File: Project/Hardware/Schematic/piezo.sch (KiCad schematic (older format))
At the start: 5 parts

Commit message: Fixa bibliotek ref
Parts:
- U?: symbol lab-rescue:piezo-PASC -> PASC:piezo
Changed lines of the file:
@@
 $EndDescr
 $Comp
-L lab-rescue:piezo-PASC U?
+L PASC:piezo U?
 U 1 1 5C5E3EC0
 P 6600 3700

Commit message: La till pins till cubemx, bytte transistor till piezo och la till footprint för accelerometer
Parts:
- removed Q?: 2SC1815, Package_TO_SOT_THT:TO-92_Inline, symbol Transistor_BJT:2SC1815
- added Q?: 2N3906, Package_TO_SOT_THT:TO-92_Inline, symbol Transistor_BJT:2N3906
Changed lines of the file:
@@
 	0    1    1    0
-$EndComp
-$Comp
-L Transistor_BJT:2SC1815 Q?
-U 1 1 5C5EB691
-P 5600 4600
-F 0 "Q?" H 5791 4646 50  0000 L CNN
-F 1 "2SC1815" H 5791 4555 50  0000 L CNN
-F 2 "Package_TO_SOT_THT:TO-92_Inline" H 5800 4525 50  0001 L CIN
-F 3 "https://media.digikey.com/pdf/Data%20Sheets/Toshiba%20PDFs/2SC1815.pdf" H 5600 4600 50  0001 L CNN
-	1    5600 4600
-	1    0    0    -1
 $EndComp
 Wire Wire Line
@@
 Text HLabel 4300 4600 0    50   Input ~ 0
 PIEZOPWM
+$Comp
+L Transistor_BJT:2N3906 Q?
+U 1 1 5C68E108
+P 5600 4600
+F 0 "Q?" H 5791 4646 50  0000 L CNN
+F 1 "2N3906" H 5791 4555 50  0000 L CNN
+F 2 "Package_TO_SOT_THT:TO-92_Inline" H 5800 4525 50  0001 L CIN
+F 3 "https://www.fairchildsemi.com/datasheets/2N/2N3906.pdf" H 5600 4600 50  0001 L CNN
+	1    5600 4600
+	1    0    0    -1
+$EndComp
 $EndSCHEMATC

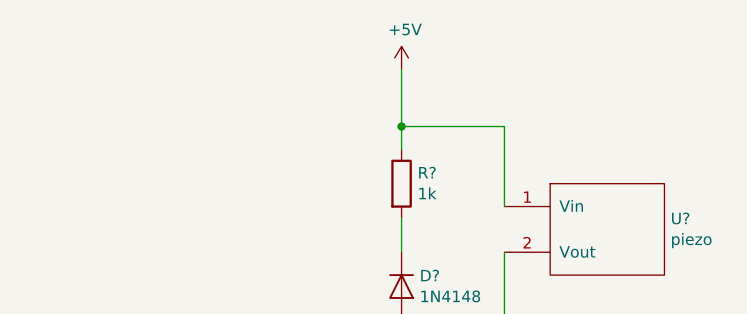
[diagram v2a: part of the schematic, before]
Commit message: Tagit bort knapp, ändrat power till piezo
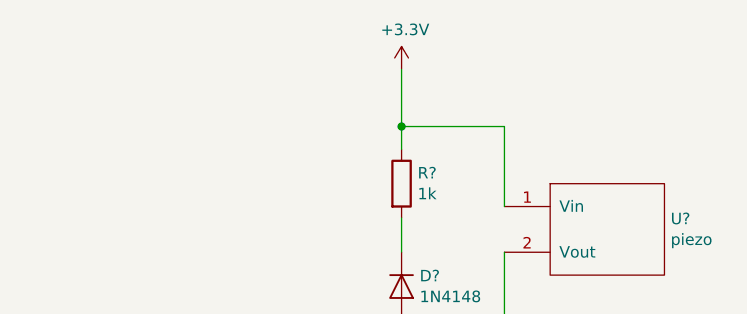
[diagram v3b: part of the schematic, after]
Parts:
- Q?: footprint Package_TO_SOT_THT:TO-92_Inline -> TO_SOT_Packages_THT:TO-92_Inline_Wide
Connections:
- net +5V renamed +3V3
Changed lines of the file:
@@
 Wire Wire Line
 	4750 4600 4300 4600
-$Comp
-L power:+5V #PWR?
-U 1 1 5C5E2E3F
-P 5700 3000
-F 0 "#PWR?" H 5700 2850 50  0001 C CNN
-F 1 "+5V" H 5715 3173 50  0000 C CNN
-F 2 "" H 5700 3000 50  0001 C CNN
-F 3 "" H 5700 3000 50  0001 C CNN
-	1    5700 3000
-	1    0    0    -1
-$EndComp
 Text HLabel 4300 4600 0    50   Input ~ 0
 PIEZOPWM
@@
 F 0 "Q?" H 5791 4646 50  0000 L CNN
 F 1 "2N3906" H 5791 4555 50  0000 L CNN
-F 2 "Package_TO_SOT_THT:TO-92_Inline" H 5800 4525 50  0001 L CIN
+F 2 "TO_SOT_Packages_THT:TO-92_Inline_Wide" H 5800 4525 50  0001 L CIN
 F 3 "https://www.fairchildsemi.com/datasheets/2N/2N3906.pdf" H 5600 4600 50  0001 L CNN
 	1    5600 4600
 	1    0    0    -1
 $EndComp
+$Comp
+L power:+3.3V #PWR?
+U 1 1 5C6DC10D
+P 5700 3000
+F 0 "#PWR?" H 5700 2850 50  0001 C CNN
+F 1 "+3.3V" H 5715 3173 50  0000 C CNN
+F 2 "" H 5700 3000 50  0001 C CNN
+F 3 "" H 5700 3000 50  0001 C CNN
+	1    5700 3000
+	1    0    0    -1
+$EndComp

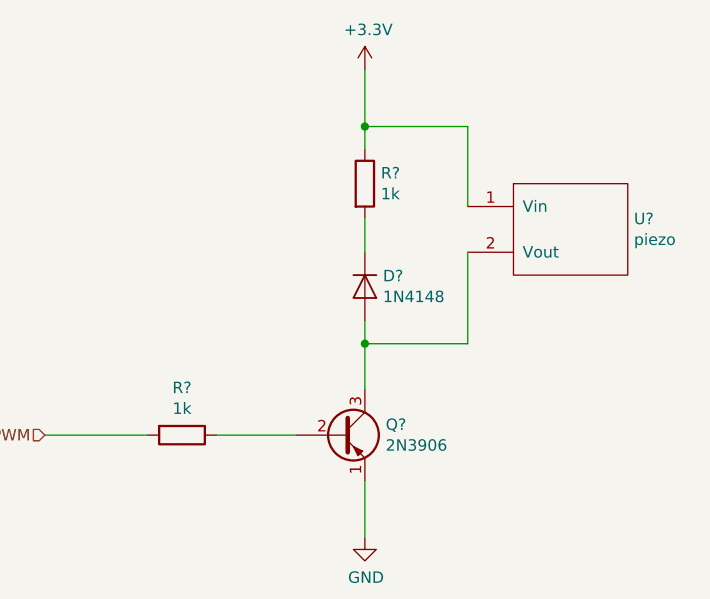
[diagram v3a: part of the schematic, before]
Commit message: Tog bort power supply +7, lade till switch för att switcha mellan batteri och USB power. Lade till power-net symbol för oregulerad supply voltage +VIN.
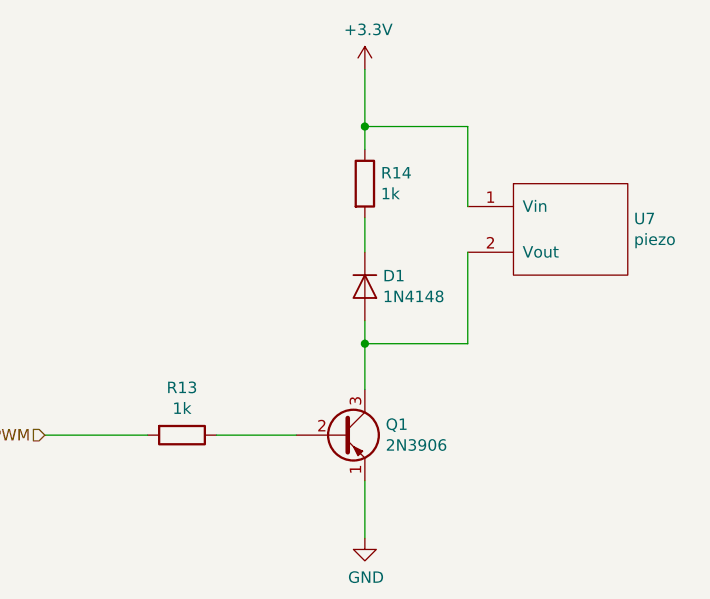
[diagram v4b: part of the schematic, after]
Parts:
- gave numbers to parts that had none: 5
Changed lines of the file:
@@
 $EndDescr
 $Comp
-L PASC:piezo U?
+L PASC:piezo U7
 U 1 1 5C5E3EC0
 P 6600 3700
-F 0 "U?" H 6877 3746 50  0000 L CNN
+F 0 "U7" H 6877 3746 50  0000 L CNN
 F 1 "piezo" H 6877 3655 50  0000 L CNN
 F 2 "PASC:Piezo" H 6600 3700 50  0001 C CNN
@@
 $EndComp
 $Comp
-L Device:R R?
+L Device:R R14
 U 1 1 5C5EB38A
 P 5700 3500
-F 0 "R?" H 5770 3546 50  0000 L CNN
+F 0 "R14" H 5770 3546 50  0000 L CNN
 F 1 "1k" H 5770 3455 50  0000 L CNN
 F 2 "" V 5630 3500 50  0001 C CNN
@@
 $EndComp
 $Comp
-L Diode:1N4148 D?
+L Diode:1N4148 D1
 U 1 1 5C5EB4E1
 P 5700 3950
-F 0 "D?" V 5654 4029 50  0000 L CNN
+F 0 "D1" V 5654 4029 50  0000 L CNN
 F 1 "1N4148" V 5745 4029 50  0000 L CNN
 F 2 "Diode_THT:D_DO-35_SOD27_P7.62mm_Horizontal" H 5700 3775 50  0001 C CNN
@@
 	5700 4200 5700 4400
 $Comp
-L Device:R R?
+L Device:R R13
 U 1 1 5C5EB823
 P 4900 4600
-F 0 "R?" V 4693 4600 50  0000 C CNN
+F 0 "R13" V 4693 4600 50  0000 C CNN
 F 1 "1k" V 4784 4600 50  0000 C CNN
 F 2 "" V 4830 4600 50  0001 C CNN
@@
 	5050 4600 5400 4600
 $Comp
-L power:GND #PWR?
+L power:GND #PWR0137
 U 1 1 5C5EB928
 P 5700 5050
-F 0 "#PWR?" H 5700 4800 50  0001 C CNN
+F 0 "#PWR0137" H 5700 4800 50  0001 C CNN
 F 1 "GND" H 5705 4877 50  0000 C CNN
 F 2 "" H 5700 5050 50  0001 C CNN
@@
 PIEZOPWM
 $Comp
-L Transistor_BJT:2N3906 Q?
+L Transistor_BJT:2N3906 Q1
 U 1 1 5C68E108
 P 5600 4600
-F 0 "Q?" H 5791 4646 50  0000 L CNN
+F 0 "Q1" H 5791 4646 50  0000 L CNN
 F 1 "2N3906" H 5791 4555 50  0000 L CNN
 F 2 "TO_SOT_Packages_THT:TO-92_Inline_Wide" H 5800 4525 50  0001 L CIN
@@
 $EndComp
 $Comp
-L power:+3.3V #PWR?
+L power:+3.3V #PWR0138
 U 1 1 5C6DC10D
 P 5700 3000
-F 0 "#PWR?" H 5700 2850 50  0001 C CNN
+F 0 "#PWR0138" H 5700 2850 50  0001 C CNN
 F 1 "+3.3V" H 5715 3173 50  0000 C CNN
 F 2 "" H 5700 3000 50  0001 C CNN

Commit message: Intermediate...
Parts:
- removed Q1: 2N3906, TO_SOT_Packages_THT:TO-92_Inline_Wide, symbol Transistor_BJT:2N3906
- added Q1: 2N3904, Package_TO_SOT_THT:TO-92_Inline_Wide, symbol Transistor_BJT:2N3904
- R13, R14: footprint (none) -> Resistor_SMD:R_0805_2012Metric_Pad1.15x1.40mm_HandSolder
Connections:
- net GND: now also Q1.1 (E)
- net at D1.2 (A), U7.2 (Vout): now also Q1.3 (C)
- net at R13.1: now also Q1.2 (B)
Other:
- moved on the sheet: D1, R13, R14, U7
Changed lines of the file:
@@
 EELAYER 26 0
 EELAYER END
-$Descr A4 11693 8268
+$Descr User 5512 5512
 encoding utf-8
 Sheet 6 7
 Title ""
-Date ""
-Rev ""
-Comp ""
+Date "2019-02-12"
+Rev "1"
+Comp "PASC"
 Comment1 ""
 Comment2 ""
@@
 L PASC:piezo U7
 U 1 1 5C5E3EC0
-P 6600 3700
-F 0 "U7" H 6877 3746 50  0000 L CNN
-F 1 "piezo" H 6877 3655 50  0000 L CNN
-F 2 "PASC:Piezo" H 6600 3700 50  0001 C CNN
-F 3 "" H 6600 3700 50  0001 C CNN
-	1    6600 3700
+P 3800 1800
+F 0 "U7" H 4077 1846 50  0000 L CNN
+F 1 "piezo" H 4077 1755 50  0000 L CNN
+F 2 "PASC:Piezo" H 3800 1800 50  0001 C CNN
+F 3 "" H 3800 1800 50  0001 C CNN
+	1    3800 1800
 	1    0    0    -1
 $EndComp
@@
 L Device:R R14
 U 1 1 5C5EB38A
-P 5700 3500
-F 0 "R14" H 5770 3546 50  0000 L CNN
-F 1 "1k" H 5770 3455 50  0000 L CNN
-F 2 "" V 5630 3500 50  0001 C CNN
-F 3 "~" H 5700 3500 50  0001 C CNN
-	1    5700 3500
+P 2900 1600
+F 0 "R14" H 2970 1646 50  0000 L CNN
+F 1 "1k" H 2970 1555 50  0000 L CNN
+F 2 "Resistor_SMD:R_0805_2012Metric_Pad1.15x1.40mm_HandSolder" V 2830 1600 50  0001 C CNN
+F 3 "~" H 2900 1600 50  0001 C CNN
+	1    2900 1600
 	1    0    0    -1
 $EndComp
@@
 L Diode:1N4148 D1
 U 1 1 5C5EB4E1
-P 5700 3950
-F 0 "D1" V 5654 4029 50  0000 L CNN
-F 1 "1N4148" V 5745 4029 50  0000 L CNN
-F 2 "Diode_THT:D_DO-35_SOD27_P7.62mm_Horizontal" H 5700 3775 50  0001 C CNN
-F 3 "http://www.nxp.com/documents/data_sheet/1N4148_1N4448.pdf" H 5700 3950 50  0001 C CNN
-	1    5700 3950
+P 2900 2050
+F 0 "D1" V 2854 2129 50  0000 L CNN
+F 1 "1N4148" V 2945 2129 50  0000 L CNN
+F 2 "Diode_THT:D_DO-35_SOD27_P7.62mm_Horizontal" H 2900 1875 50  0001 C CNN
+F 3 "http://www.nxp.com/documents/data_sheet/1N4148_1N4448.pdf" H 2900 2050 50  0001 C CNN
+	1    2900 2050
 	0    1    1    0
 $EndComp
 Wire Wire Line
-	5700 3000 5700 3250
+	2900 1100 2900 1350
 Wire Wire Line
-	5700 3650 5700 3800
+	2900 1750 2900 1900
 Wire Wire Line
-	5700 4100 5700 4200
+	2900 2200 2900 2300
 Wire Wire Line
-	6150 3600 6150 3250
+	3350 1700 3350 1350
 Wire Wire Line
-	6150 3250 5700 3250
-Connection ~ 5700 3250
+	3350 1350 2900 1350
+Connection ~ 2900 1350
 Wire Wire Line
-	5700 3250 5700 3350
+	2900 1350 2900 1450
 Wire Wire Line
-	6150 3800 6150 4200
+	3350 1900 3350 2300
 Wire Wire Line
-	6150 4200 5700 4200
-Connection ~ 5700 4200
+	3350 2300 2900 2300
+Connection ~ 2900 2300
 Wire Wire Line
-	5700 4200 5700 4400
+	2900 2300 2900 2500
 $Comp
 L Device:R R13
 U 1 1 5C5EB823
-P 4900 4600
-F 0 "R13" V 4693 4600 50  0000 C CNN
-F 1 "1k" V 4784 4600 50  0000 C CNN
-F 2 "" V 4830 4600 50  0001 C CNN
-F 3 "~" H 4900 4600 50  0001 C CNN
-	1    4900 4600
+P 2100 2700
+F 0 "R13" V 1893 2700 50  0000 C CNN
+F 1 "1k" V 1984 2700 50  0000 C CNN
+F 2 "Resistor_SMD:R_0805_2012Metric_Pad1.15x1.40mm_HandSolder" V 2030 2700 50  0001 C CNN
+F 3 "~" H 2100 2700 50  0001 C CNN
+	1    2100 2700
 	0    1    1    0
 $EndComp
 Wire Wire Line
-	5050 4600 5400 4600
+	2250 2700 2600 2700
 $Comp
 L power:GND #PWR0137
 U 1 1 5C5EB928
-P 5700 5050
-F 0 "#PWR0137" H 5700 4800 50  0001 C CNN
-F 1 "GND" H 5705 4877 50  0000 C CNN
-F 2 "" H 5700 5050 50  0001 C CNN
-F 3 "" H 5700 5050 50  0001 C CNN
-	1    5700 5050
+P 2900 3150
+F 0 "#PWR0137" H 2900 2900 50  0001 C CNN
+F 1 "GND" H 2905 2977 50  0000 C CNN
+F 2 "" H 2900 3150 50  0001 C CNN
+F 3 "" H 2900 3150 50  0001 C CNN
+	1    2900 3150
 	1    0    0    -1
 $EndComp
 Wire Wire Line
-	5700 4800 5700 5050
+	2900 2900 2900 3150
 Wire Wire Line
-	4750 4600 4300 4600
-Text HLabel 4300 4600 0    50   Input ~ 0
+	1950 2700 1500 2700
+Text HLabel 1500 2700 0    50   Input ~ 0
 PIEZOPWM
 $Comp
-L Transistor_BJT:2N3906 Q1
-U 1 1 5C68E108
-P 5600 4600
-F 0 "Q1" H 5791 4646 50  0000 L CNN
-F 1 "2N3906" H 5791 4555 50  0000 L CNN
-F 2 "TO_SOT_Packages_THT:TO-92_Inline_Wide" H 5800 4525 50  0001 L CIN
-F 3 "https://www.fairchildsemi.com/datasheets/2N/2N3906.pdf" H 5600 4600 50  0001 L CNN
-	1    5600 4600
+L power:+3.3V #PWR0138
+U 1 1 5C6DC10D
+P 2900 1100
+F 0 "#PWR0138" H 2900 950 50  0001 C CNN
+F 1 "+3.3V" H 2915 1273 50  0000 C CNN
+F 2 "" H 2900 1100 50  0001 C CNN
+F 3 "" H 2900 1100 50  0001 C CNN
+	1    2900 1100
 	1    0    0    -1
 $EndComp
 $Comp
-L power:+3.3V #PWR0138
-U 1 1 5C6DC10D
-P 5700 3000
-F 0 "#PWR0138" H 5700 2850 50  0001 C CNN
-F 1 "+3.3V" H 5715 3173 50  0000 C CNN
-F 2 "" H 5700 3000 50  0001 C CNN
-F 3 "" H 5700 3000 50  0001 C CNN
-	1    5700 3000
+L Transistor_BJT:2N3904 Q1
+U 1 1 5C64EC5C
+P 2800 2700
+F 0 "Q1" H 2991 2746 50  0000 L CNN
+F 1 "2N3904" H 2991 2655 50  0000 L CNN
+F 2 "Package_TO_SOT_THT:TO-92_Inline_Wide" H 3000 2625 50  0001 L CIN
+F 3 "https://www.fairchildsemi.com/datasheets/2N/2N3904.pdf" H 2800 2700 50  0001 L CNN
+	1    2800 2700
 	1    0    0    -1
 $EndComp
